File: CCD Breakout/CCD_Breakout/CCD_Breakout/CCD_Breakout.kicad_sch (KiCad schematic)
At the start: 2 parts

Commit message: Fixed CCD Footprints
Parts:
- H1, H2: footprint (none) -> MRDT_Drill_Holes:4_40_Hole_Corner
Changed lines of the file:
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@@
 			)
 		)
-		(property "Footprint" ""
+		(property "Footprint" "MRDT_Drill_Holes:4_40_Hole_Corner"
 			(at 275.59 17.78 0)
 			(effects
@@
 			)
 		)
-		(property "Footprint" ""
+		(property "Footprint" "MRDT_Drill_Holes:4_40_Hole_Corner"
 			(at 255.27 17.78 0)
 			(effects

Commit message: Initial layout
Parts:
- H1, H2: footprint MRDT_Drill_Holes:4_40_Hole_Corner -> MRDT_Drill_Holes:4_40_Hole
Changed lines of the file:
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@@
 			)
 		)
-		(property "Footprint" "MRDT_Drill_Holes:4_40_Hole_Corner"
+		(property "Footprint" "MRDT_Drill_Holes:4_40_Hole"
 			(at 275.59 17.78 0)
 			(effects
@@
 			)
 		)
-		(property "Footprint" "MRDT_Drill_Holes:4_40_Hole_Corner"
+		(property "Footprint" "MRDT_Drill_Holes:4_40_Hole"
 			(at 255.27 17.78 0)
 			(effects

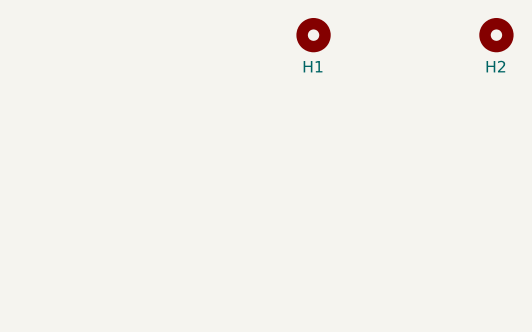
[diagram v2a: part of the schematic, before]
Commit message: Board redesign for laser engraving
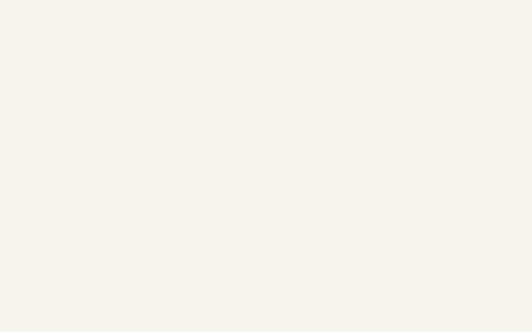
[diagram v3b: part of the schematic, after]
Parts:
- removed H1, H2: ~, MRDT_Drill_Holes:4_40_Hole, symbol Mechanical:MountingHole
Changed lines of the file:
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@@
-		)
-	)
-	(symbol
-		(lib_id "Mechanical:MountingHole")
-		(at 275.59 17.78 0)
-		(unit 1)
-		(exclude_from_sim no)
-		(in_bom no)
-		(on_board yes)
-		(dnp no)
-		(property "Reference" "H2"
-			(at 274.32 21.336 0)
-			(effects
-				(font
-					(size 1.27 1.27)
-				)
-				(justify left)
-			)
-		)
-		(property "Value" "~"
-			(at 275.082 20.066 0)
-			(effects
-				(font
-					(size 1.27 1.27)
-				)
-				(justify left)
-			)
-		)
-		(property "Footprint" "MRDT_Drill_Holes:4_40_Hole"
-			(at 275.59 17.78 0)
-			(effects
-				(font
-					(size 1.27 1.27)
-				)
-				(hide yes)
-			)
-		)
-		(property "Datasheet" "~"
-			(at 275.59 17.78 0)
-			(effects
-				(font
-					(size 1.27 1.27)
-				)
-				(hide yes)
-			)
-		)
-		(property "Description" "Mounting Hole without connection"
-			(at 275.59 17.78 0)
-			(effects
-				(font
-					(size 1.27 1.27)
-				)
-				(hide yes)
-			)
-		)
-		(instances
-			(project "CCD_Breakout"
-				(path "/102965ac-29c6-4f96-94a4-d07431f6d693"
-					(reference "H2")
-					(unit 1)
-				)
-			)
-		)
-	)
-	(symbol
-		(lib_id "Mechanical:MountingHole")
-		(at 255.27 17.78 0)
-		(unit 1)
-		(exclude_from_sim no)
-		(in_bom no)
-		(on_board yes)
-		(dnp no)
-		(property "Reference" "H1"
-			(at 254 21.336 0)
-			(effects
-				(font
-					(size 1.27 1.27)
-				)
-				(justify left)
-			)
-		)
-		(property "Value" "~"
-			(at 254.762 20.066 0)
-			(effects
-				(font
-					(size 1.27 1.27)
-				)
-				(justify left)
-			)
-		)
-		(property "Footprint" "MRDT_Drill_Holes:4_40_Hole"
-			(at 255.27 17.78 0)
-			(effects
-				(font
-					(size 1.27 1.27)
-				)
-				(hide yes)
-			)
-		)
-		(property "Datasheet" "~"
-			(at 255.27 17.78 0)
-			(effects
-				(font
-					(size 1.27 1.27)
-				)
-				(hide yes)
-			)
-		)
-		(property "Description" "Mounting Hole without connection"
-			(at 255.27 17.78 0)
-			(effects
-				(font
-					(size 1.27 1.27)
-				)
-				(hide yes)
-			)
-		)
-		(instances
-			(project ""
-				(path "/102965ac-29c6-4f96-94a4-d07431f6d693"
-					(reference "H1")
-					(unit 1)
-				)
-			)
 		)
 	)
